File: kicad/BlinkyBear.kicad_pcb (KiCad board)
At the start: 2 copper layers, 44.6 x 53.6 mm, 9 parts, among them SW1 SW_SPDT

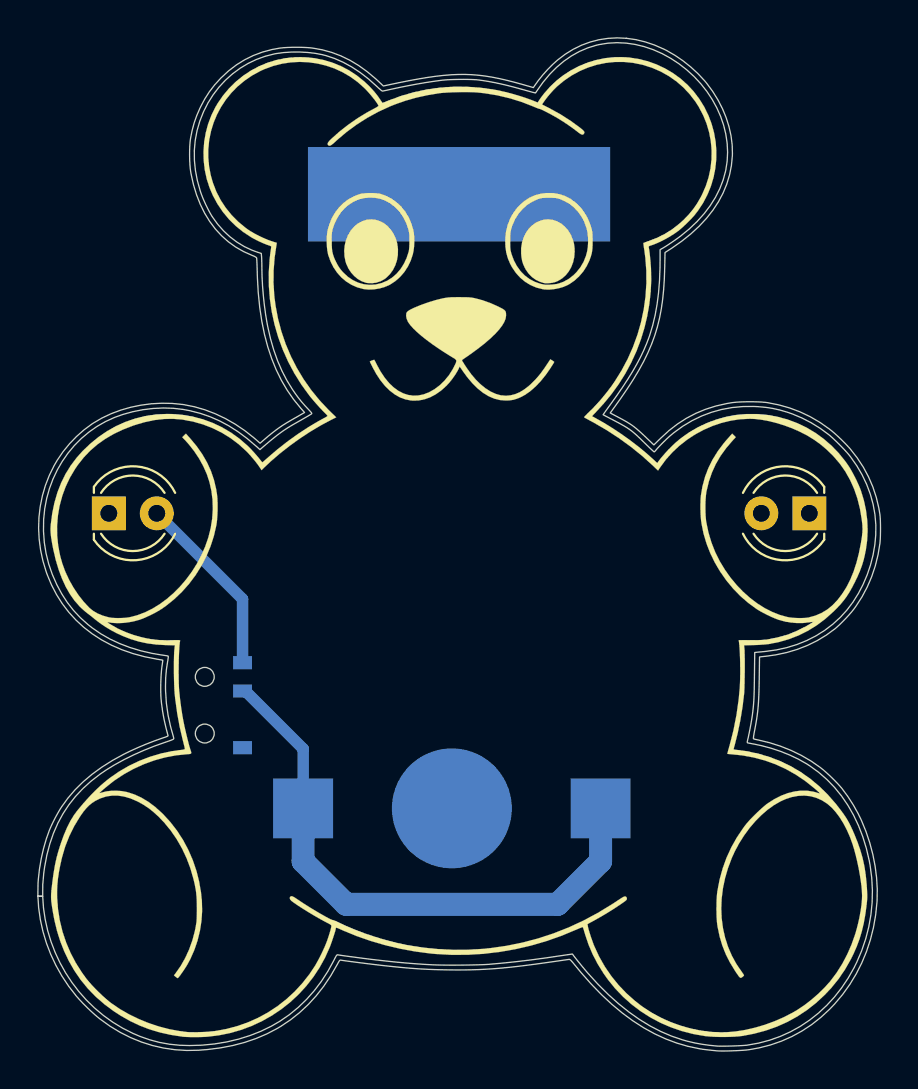
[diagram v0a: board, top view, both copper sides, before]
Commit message: Updates and adds a BOM
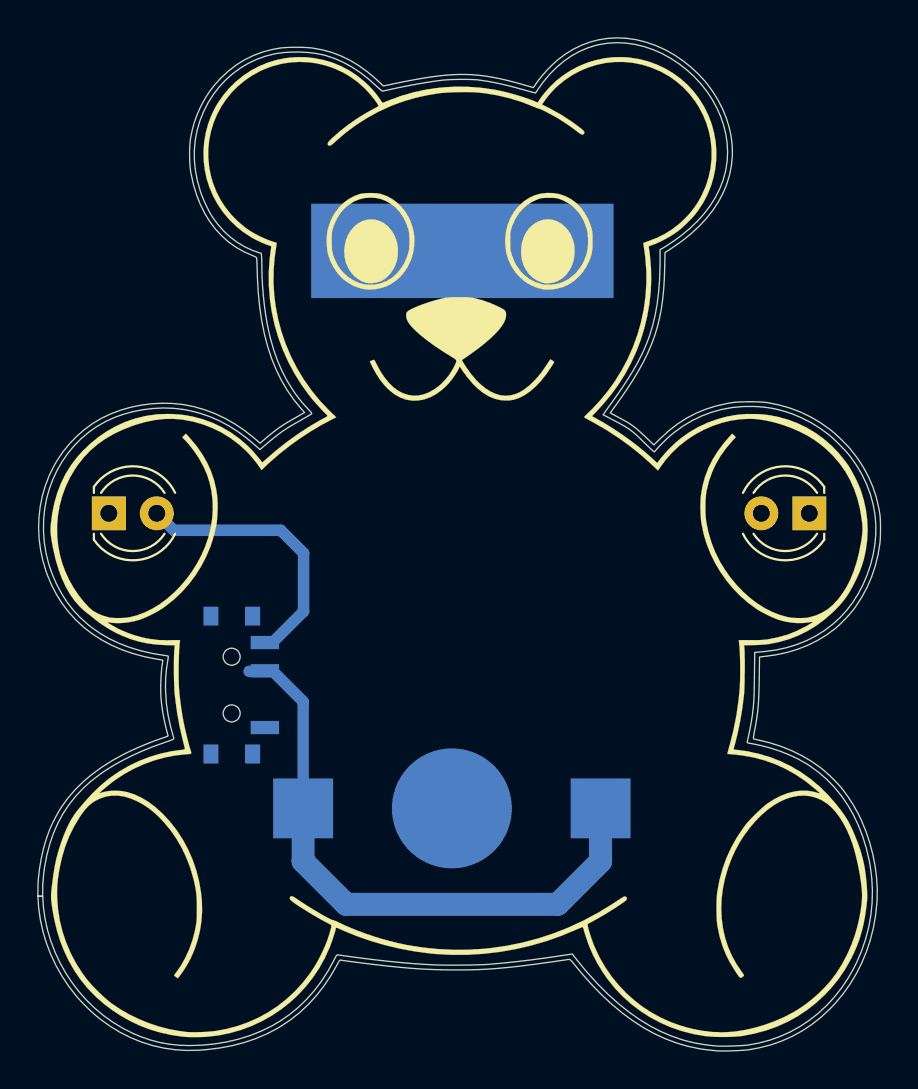
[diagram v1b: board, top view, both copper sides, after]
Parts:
- SW1: footprint blinky-bear:Micro_Schiebeschalter -> Buttons_Switches_SMD:SW_SPDT_PCM12
- moved REF** 3.00 mm to (136.1, 64.8)
- moved SW1 2.05 mm to (124.2, 87.8), turned to 90 degrees
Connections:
- SW1 pad 1: (no net) -> Net-(SW1-Pad1)
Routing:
- net Net-(D1-Pad2): track 9.79 -> 14.5 mm
- net /V+: track 30.9 -> 32.4 mm
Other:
- board text added: "Blinky Bear 2L_2"
- board text removed: "Blinky Bear 2L_1"

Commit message: Refreshed to KiCad 8
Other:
- net class Default removed
